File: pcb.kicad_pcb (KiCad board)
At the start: 2 copper layers, 120.7 x 70.6 mm, 37 parts, among them SW1 SW_Push, SW2 SW_Push, U1 Pico

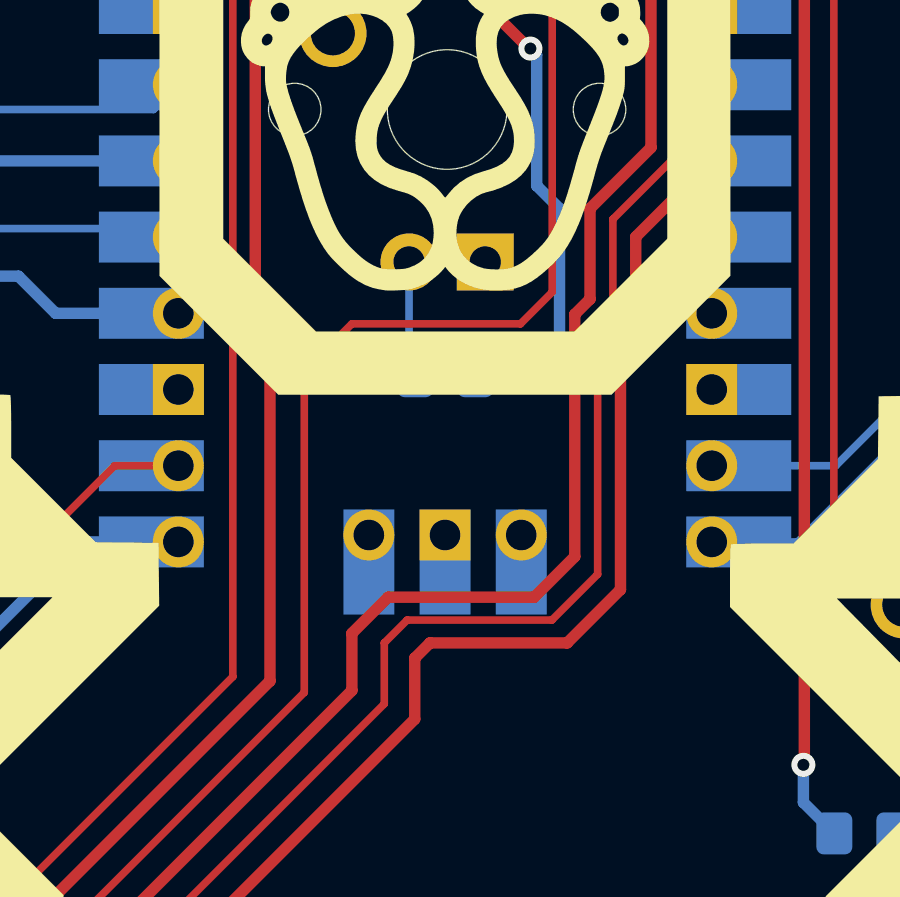
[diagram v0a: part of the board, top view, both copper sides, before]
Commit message: Move R8 to allow for surface mounting the Pico
Not recommended, but you can if you really want to now. Also updated the design rules to fit JLCPCB manufacturing specs.
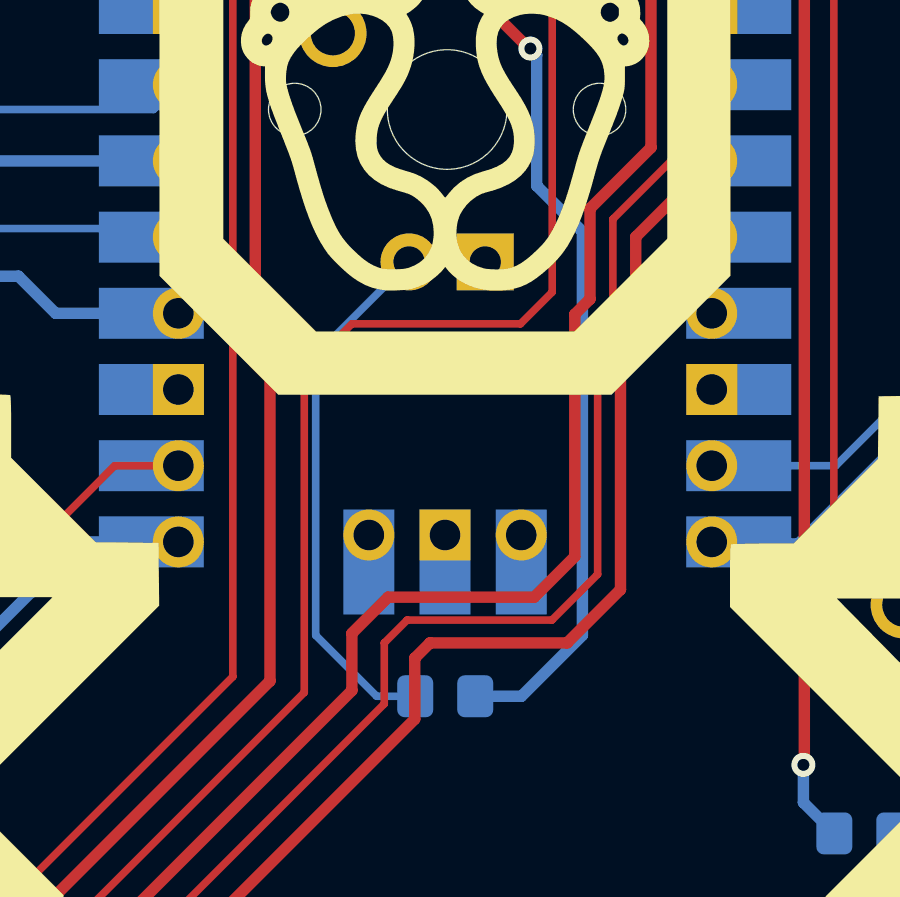
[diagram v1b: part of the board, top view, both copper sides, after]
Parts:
- moved R8 10.7 mm to (173.0, 114.8)
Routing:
- net Net-(MX8-Pad3): track 3.90 -> 17.9 mm
- net P2 CN LED: track 40.6 -> 51.9 mm
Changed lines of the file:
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@@
   )
   (footprint "Resistor_SMD:R_0805_2012Metric_Pad1.20x1.40mm_HandSolder" (layer "B.Cu")
-    (at 172.974 104.14 180)
+    (at 172.974 114.808 180)
     (descr "Resistor SMD 0805 (2012 Metric), square (rectangular) end terminal, IPC_7351 nominal with elongated pad for handsoldering. (Body size source: IPC-SM-782 page 72, https://www.pcb-3d.com/wordpress/wp-content/uploads/ipc-sm-782a_amendment_1_and_2.pdf), generated with kicad-footprint-generator")
     (tags "resistor handsolder")
@@
   (segment (start 175.768 93.218) (end 173.0375 90.4875) (width 0.381) (layer "F.Cu") (net 16))
   (via (at 175.813 93.218) (size 0.8) (drill 0.4) (layers "F.Cu" "B.Cu") (net 16))
-  (segment (start 176.784 102.87) (end 175.514 104.14) (width 0.381) (layer "B.Cu") (net 16))
+  (segment (start 177.546 99.314) (end 177.546 112.776) (width 0.381) (layer "B.Cu") (net 16))
   (segment (start 175.813 93.218) (end 176.022 93.427) (width 0.381) (layer "B.Cu") (net 16))
-  (segment (start 176.784 98.552) (end 176.784 102.87) (width 0.381) (layer "B.Cu") (net 16))
-  (segment (start 176.022 97.79) (end 176.784 98.552) (width 0.381) (layer "B.Cu") (net 16))
+  (segment (start 177.546 112.776) (end 175.514 114.808) (width 0.381) (layer "B.Cu") (net 16))
   (segment (start 176.022 93.427) (end 176.022 97.79) (width 0.381) (layer "B.Cu") (net 16))
-  (segment (start 175.514 104.14) (end 173.974 104.14) (width 0.381) (layer "B.Cu") (net 16))
+  (segment (start 176.022 97.79) (end 177.546 99.314) (width 0.381) (layer "B.Cu") (net 16))
+  (segment (start 175.514 114.808) (end 173.974 114.808) (width 0.381) (layer "B.Cu") (net 16))
   (segment (start 183.145999 61.402998) (end 181.85775 61.402998) (width 0.254) (layer "F.Cu") (net 17))
   (segment (start 186.436 71.696248) (end 186.436 64.692999) (width 0.254) (layer "F.Cu") (net 17))
@@
   (segment (start 152.7175 81.28) (end 152.7175 84.8835) (width 0.381) (layer "B.Cu") (net 43))
   (segment (start 152.7175 84.8835) (end 152.924 85.09) (width 0.381) (layer "B.Cu") (net 43))
-  (segment (start 171.974 104.14) (end 171.7675 103.9335) (width 0.254) (layer "B.Cu") (net 44))
-  (segment (start 171.7675 103.9335) (end 171.7675 100.33) (width 0.254) (layer "B.Cu") (net 44))
+  (segment (start 168.656 103.4415) (end 171.7675 100.33) (width 0.254) (layer "B.Cu") (net 44))
+  (segment (start 170.688 114.808) (end 168.656 112.776) (width 0.254) (layer "B.Cu") (net 44))
+  (segment (start 171.974 114.808) (end 170.688 114.808) (width 0.254) (layer "B.Cu") (net 44))
+  (segment (start 168.656 112.776) (end 168.656 103.4415) (width 0.254) (layer "B.Cu") (net 44))
   (segment (start 193.278 84.312) (end 190.8175 81.8515) (width 0.254) (layer "B.Cu") (net 45))
   (segment (start 190.8175 82.1055) (end 190.8175 81.28) (width 0.254) (layer "B.Cu") (net 45))

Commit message: we only want 8 WS2812Bs
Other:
- board text added: "WS2812B (8 LEDs)"
- board text removed: "WS2812B (10 LEDs)"
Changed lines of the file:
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@@
     (effects (font (size 0.8 0.8) (thickness 0.15)) (justify mirror))
   )
-  (gr_text "WS2812B\n(10 LEDs)" (at 92.075 89.662) (layer "B.SilkS")
+  (gr_text "WS2812B\n(8 LEDs)" (at 92.075 89.662) (layer "B.SilkS")
     (effects (font (size 1 1) (thickness 0.15)) (justify mirror))
   )

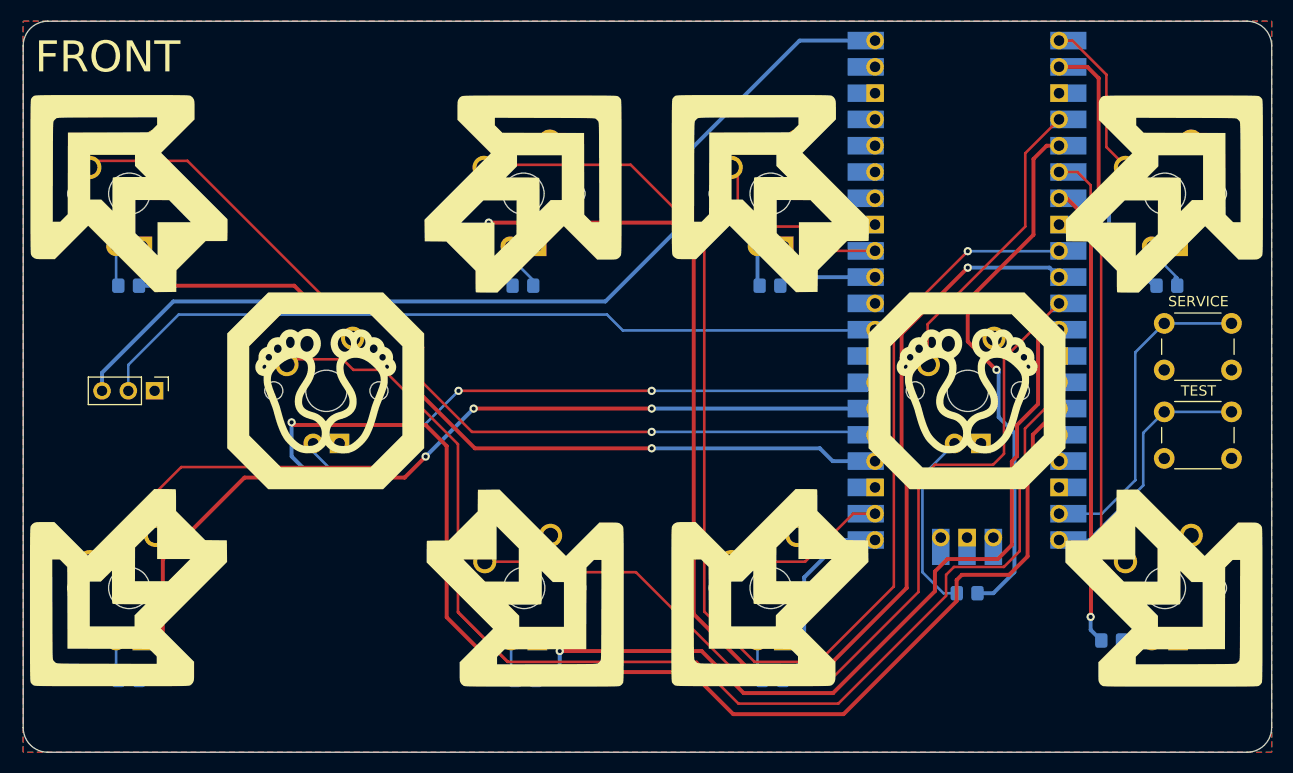
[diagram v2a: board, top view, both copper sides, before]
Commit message: Add WS2812B footprints, various tweaks
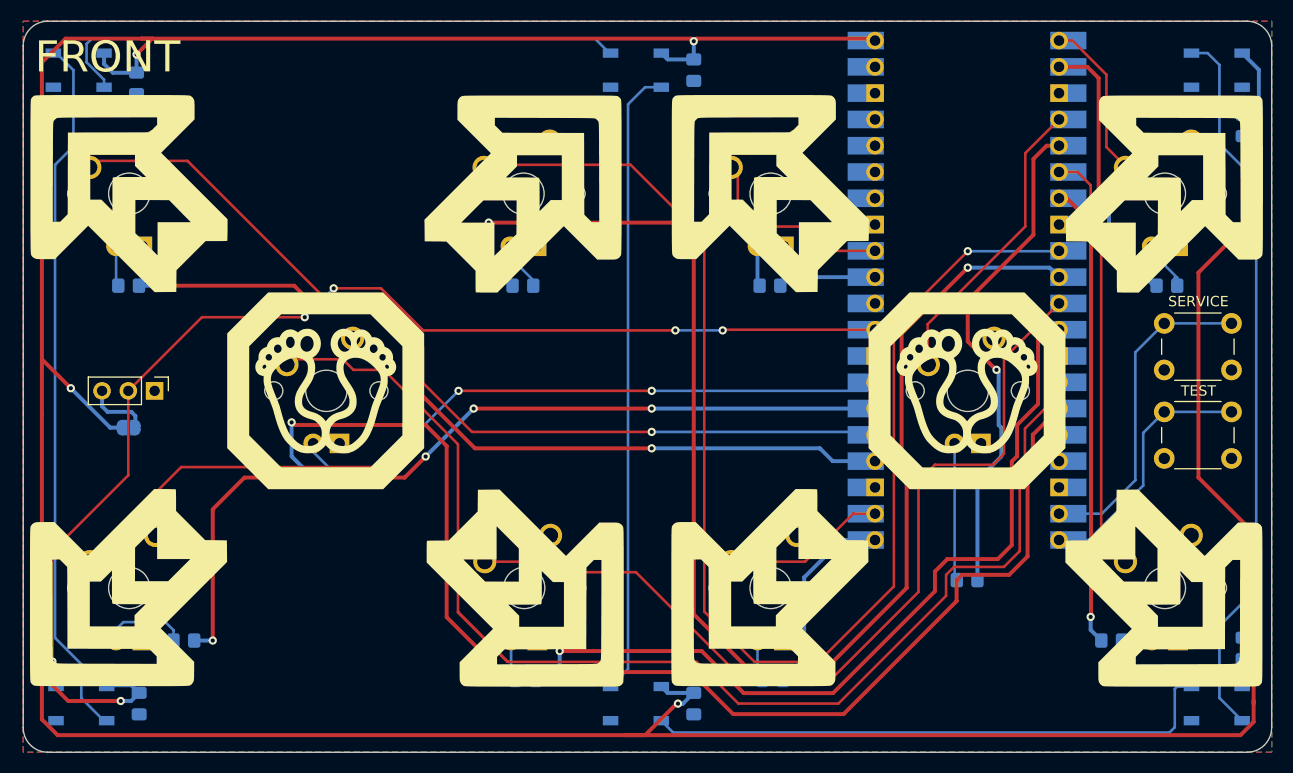
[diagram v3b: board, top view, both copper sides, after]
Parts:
- removed the G*** at (198.1, 125.7)
- added C1: 1000uF, Capacitor_SMD:C_0805_2012Metric_Pad1.18x1.45mm_HandSolder, B.Cu at (93.0, 125.5)
- added C2: 1000uF, Capacitor_SMD:C_0805_2012Metric_Pad1.18x1.45mm_HandSolder, B.Cu at (92.7, 65.5)
- added C3: 1000uF, Capacitor_SMD:C_0805_2012Metric_Pad1.18x1.45mm_HandSolder, B.Cu at (146.6, 64.3)
- added C4: 1000uF, Capacitor_SMD:C_0805_2012Metric_Pad1.18x1.45mm_HandSolder, B.Cu at (146.6, 125.5)
- added C5: 1000uF, Capacitor_SMD:C_0805_2012Metric_Pad1.18x1.45mm_HandSolder, B.Cu at (199.6, 69.6)
- added C6: 1000uF, Capacitor_SMD:C_0805_2012Metric_Pad1.18x1.45mm_HandSolder, B.Cu at (199.6, 120.1)
- added G***: LOGO, LogoFootprints:Arrow_3mm, B.Cu at (191.3, 125.7)
- added LED1: WS2812B, LED_SMD:LED_WS2812B_PLCC4_5.0x5.0mm_P3.2mm, B.Cu at (87.4, 125.5)
- added LED2: WS2812B, LED_SMD:LED_WS2812B_PLCC4_5.0x5.0mm_P3.2mm, B.Cu at (87.1, 64.3)
- added LED3: WS2812B, LED_SMD:LED_WS2812B_PLCC4_5.0x5.0mm_P3.2mm, B.Cu at (141.0, 64.3)
- added LED4: WS2812B, LED_SMD:LED_WS2812B_PLCC4_5.0x5.0mm_P3.2mm, B.Cu at (141.0, 125.5)
- added LED5: WS2812B, LED_SMD:LED_WS2812B_PLCC4_5.0x5.0mm_P3.2mm, B.Cu at (197.1, 125.5)
- added LED6: WS2812B, LED_SMD:LED_WS2812B_PLCC4_5.0x5.0mm_P3.2mm, B.Cu at (197.1, 64.3)
- added REF**: SolderJumper-2_P1.3mm_Open_RoundedPad1.0x1.5mm, Jumper:SolderJumper-2_P1.3mm_Open_RoundedPad1.0x1.5mm, B.Cu at (91.9, 98.8)
- moved R2 6.54 mm to (97.3, 119.4)
- moved R8 1.27 mm to (173.0, 113.5)
- renumbered R2 to R1, R1 to R2
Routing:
- net +5V: track 93.5 -> 396.5 mm, vias 0 -> 7
- net WS2812B 5-6: track 0.00 -> 70.4 mm
- net WS2812B 1-2: track 0.00 -> 68.5 mm
- net WS2812B 3-4: track 0.00 -> 60.9 mm
- net WS2812B 2-3: track 0.00 -> 56.3 mm
- net WS2812B 4-5: track 0.00 -> 55.7 mm
- net WS2812B DIN: track 77.3 -> 109.7 mm, vias 0 -> 5
- net P1 UL LED: track 88.1 -> 82.5 mm
- net Net-(MX8-Pad3): track 17.9 -> 13.3 mm
- net Net-(MX1-Pad3): track 3.90 -> 8.23 mm
- net P2 CN LED: track 51.9 -> 48.7 mm
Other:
- board text added: "Strip Enable"
- board text added: "WS2812B (5 LEDs)"
- board text removed: "WS2812B (8 LEDs)"

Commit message: Fix 1 typo
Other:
- board text added: "WS2812B (6 LEDs)"
- board text removed: "WS2812B (5 LEDs)"
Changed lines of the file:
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@@
     (effects (font (size 0.8 0.8) (thickness 0.15)) (justify mirror))
   )
-  (gr_text "WS2812B\n(5 LEDs)" (at 92.075 89.662) (layer "B.SilkS")
+  (gr_text "WS2812B\n(6 LEDs)" (at 92.075 89.662) (layer "B.SilkS")
     (effects (font (size 1 1) (thickness 0.15)) (justify mirror))
   )
